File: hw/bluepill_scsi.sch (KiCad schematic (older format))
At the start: 14 parts, among them J1 Micro_SD_Card, J2 Conn_02x25_Odd_Even, J3 Programming Pins, J4 Berg Power Connector, U1 BluePill_STM32F103C

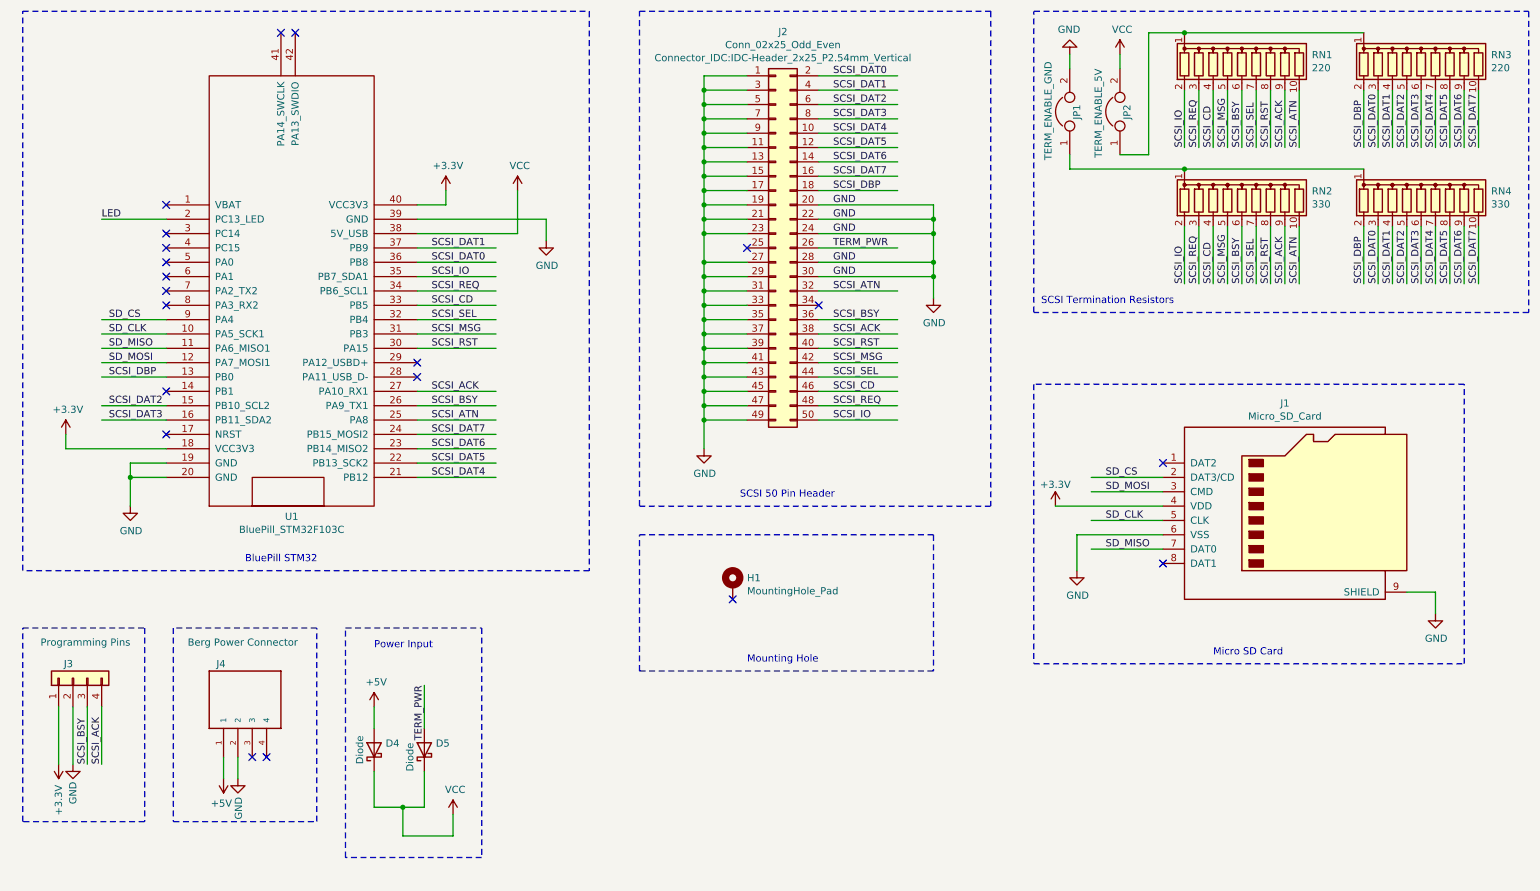
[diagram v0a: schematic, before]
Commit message: Added rough cut of STM32
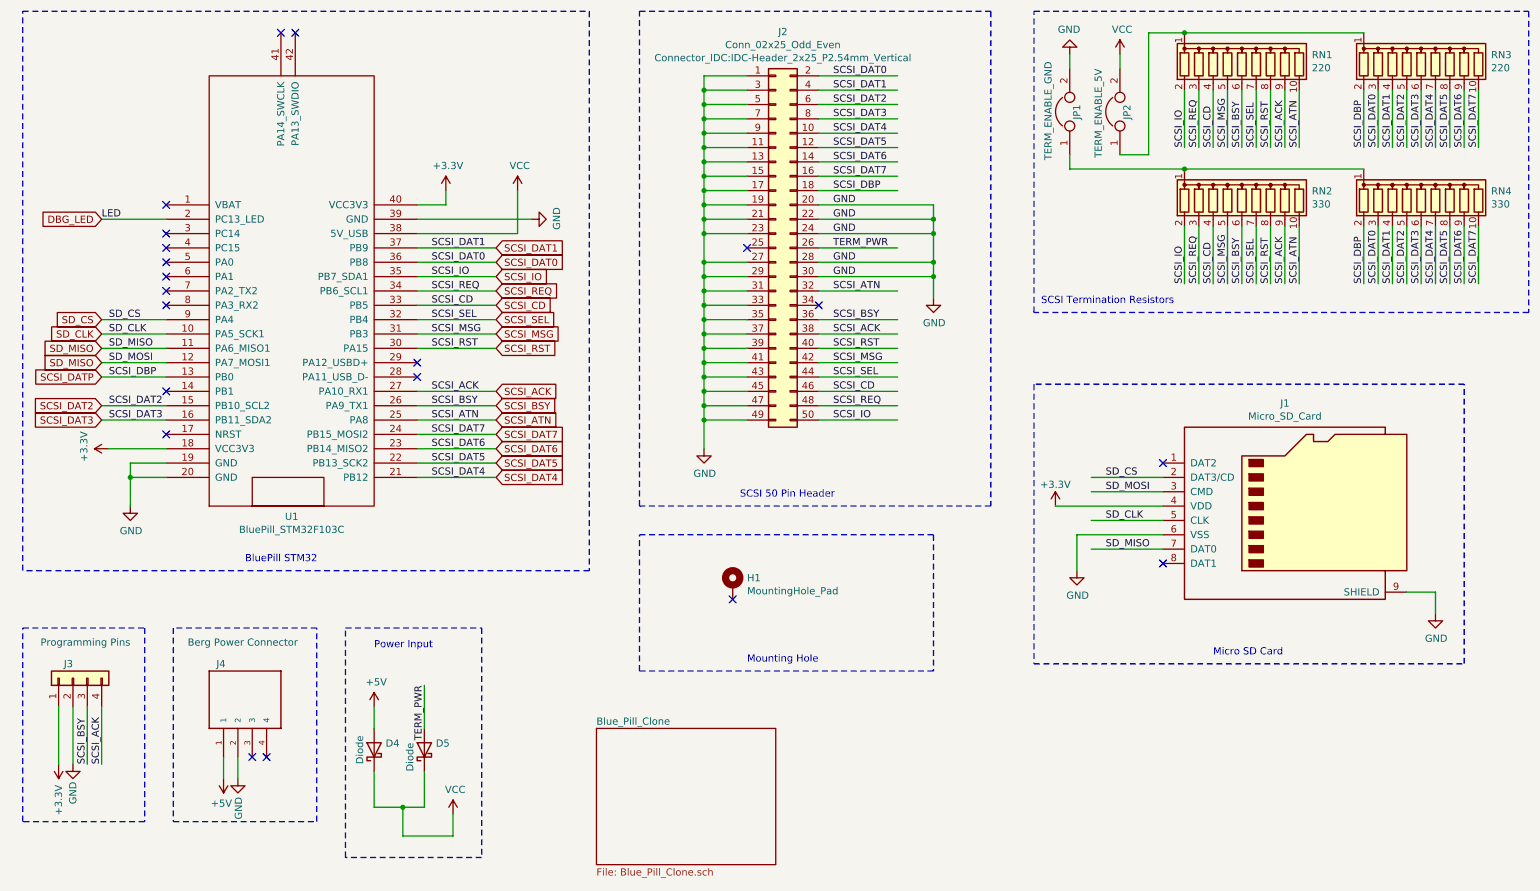
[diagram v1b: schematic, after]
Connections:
- net labels added: DBG_LED, SCSI_DATP
- wire segments 181 -> 179
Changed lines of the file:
@@
 $Descr A4 11693 8268
 encoding utf-8
-Sheet 1 1
+Sheet 1 2
 Title ""
 Date ""
@@
 	3550 2050 3550 1950
 Wire Wire Line
-	3350 2150 4250 2150
-Wire Wire Line
-	4250 2150 4250 2300
+	3350 2150 4150 2150
 $Comp
 L power:GND #PWR0104
 U 1 1 5F05BD87
-P 4250 2300
-F 0 "#PWR0104" H 4250 2050 50  0001 C CNN
-F 1 "GND" H 4255 2127 50  0000 C CNN
-F 2 "" H 4250 2300 50  0001 C CNN
-F 3 "" H 4250 2300 50  0001 C CNN
-	1    4250 2300
-	1    0    0    -1
+P 4150 2150
+F 0 "#PWR0104" H 4150 1900 50  0001 C CNN
+F 1 "GND" H 4155 1977 50  0000 C CNN
+F 2 "" H 4150 2150 50  0001 C CNN
+F 3 "" H 4150 2150 50  0001 C CNN
+	1    4150 2150
+	0    -1   -1   0
 $EndComp
 $Comp
@@
 	1    0    0    -1
 $EndComp
-Wire Wire Line
-	1600 3750 900  3750
-Wire Wire Line
-	900  3750 900  3650
 $Comp
 L power:+3.3V #PWR0107
 U 1 1 5F05ECF2
-P 900 3650
-F 0 "#PWR0107" H 900 3500 50  0001 C CNN
-F 1 "+3.3V" H 915 3823 50  0000 C CNN
-F 2 "" H 900 3650 50  0001 C CNN
-F 3 "" H 900 3650 50  0001 C CNN
-	1    900  3650
-	1    0    0    -1
+P 1200 3750
+F 0 "#PWR0107" H 1200 3600 50  0001 C CNN
+F 1 "+3.3V" H 1215 3923 50  0000 C CNN
+F 2 "" H 1200 3750 50  0001 C CNN
+F 3 "" H 1200 3750 50  0001 C CNN
+	1    1200 3750
+	0    -1   -1   0
 $EndComp
 Wire Wire Line
@@
 $EndComp
 $Comp
-L power:VCC #PWR?
+L power:VCC #PWR0112
 U 1 1 60659E21
 P 8250 1000
-F 0 "#PWR?" H 8250 850 50  0001 C CNN
+F 0 "#PWR0112" H 8250 850 50  0001 C CNN
 F 1 "VCC" H 8265 1173 50  0000 C CNN
 F 2 "" H 8250 1000 50  0001 C CNN
@@
 Wire Wire Line
 	8250 1000 8250 1100
+$Sheet
+S 4600 5700 1250 950
+U 60A49332
+F0 "Blue_Pill_Clone" 50
+F1 "Blue_Pill_Clone.sch" 50
+$EndSheet
+Text GLabel 3900 2350 2    50   Input ~ 0
+SCSI_DAT1
+Text GLabel 3900 2450 2    50   Input ~ 0
+SCSI_DAT0
+Text GLabel 3900 2550 2    50   Input ~ 0
+SCSI_IO
+Text GLabel 3900 2650 2    50   Input ~ 0
+SCSI_REQ
+Text GLabel 3900 2750 2    50   Input ~ 0
+SCSI_CD
+Text GLabel 3900 2850 2    50   Input ~ 0
+SCSI_SEL
+Text GLabel 3900 2950 2    50   Input ~ 0
+SCSI_MSG
+Text GLabel 3900 3050 2    50   Input ~ 0
+SCSI_RST
+Text GLabel 3900 3350 2    50   Input ~ 0
+SCSI_ACK
+Text GLabel 3900 3450 2    50   Input ~ 0
+SCSI_BSY
+Text GLabel 3900 3550 2    50   Input ~ 0
+SCSI_ATN
+Text GLabel 3900 3650 2    50   Input ~ 0
+SCSI_DAT7
+Text GLabel 3900 3750 2    50   Input ~ 0
+SCSI_DAT6
+Text GLabel 3900 3850 2    50   Input ~ 0
+SCSI_DAT5
+Text GLabel 3900 3950 2    50   Input ~ 0
+SCSI_DAT4
+Text GLabel 1150 2850 0    50   Input ~ 0
+SD_CS
+Text GLabel 1150 2950 0    50   Input ~ 0
+SD_CLK
+Text GLabel 1150 3050 0    50   Input ~ 0
+SD_MISO
+Text GLabel 1150 3150 0    50   Input ~ 0
+SD_MISO
+Text GLabel 1150 3250 0    50   Input ~ 0
+SCSI_DATP
+Text GLabel 1150 3450 0    50   Input ~ 0
+SCSI_DAT2
+Text GLabel 1150 3550 0    50   Input ~ 0
+SCSI_DAT3
+Wire Wire Line
+	1200 3750 1600 3750
+Text GLabel 1150 2150 0    50   Input ~ 0
+DBG_LED
 $EndSCHEMATC

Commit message: Updated bluepill all-in-one
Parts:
- renumbered D4 to D3, D5 to D4, J3 to J1, J2 to J5, J1 to J6, U1 to U3
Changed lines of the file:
@@
 $EndDescr
 $Comp
-L Connector_Generic:Conn_02x25_Odd_Even J2
+L Connector_Generic:Conn_02x25_Odd_Even J5
 U 1 1 5F0261A7
 P 5850 2350
-F 0 "J2" H 5900 3857 50  0000 C CNN
+F 0 "J5" H 5900 3857 50  0000 C CNN
 F 1 "Conn_02x25_Odd_Even" H 5900 3766 50  0000 C CNN
 F 2 "Connector_IDC:IDC-Header_2x25_P2.54mm_Vertical" H 5900 3675 50  0000 C CNN
@@
 	1350 3950 1350 4150
 $Comp
-L power:GND #PWR0102
+L power:GND #PWR04
 U 1 1 5F054918
 P 1350 4150
-F 0 "#PWR0102" H 1350 3900 50  0001 C CNN
+F 0 "#PWR04" H 1350 3900 50  0001 C CNN
 F 1 "GND" H 1355 3977 50  0000 C CNN
 F 2 "" H 1350 4150 50  0001 C CNN
@@
 	3350 2150 4150 2150
 $Comp
-L power:GND #PWR0104
+L power:GND #PWR011
 U 1 1 5F05BD87
 P 4150 2150
-F 0 "#PWR0104" H 4150 1900 50  0001 C CNN
+F 0 "#PWR011" H 4150 1900 50  0001 C CNN
 F 1 "GND" H 4155 1977 50  0000 C CNN
 F 2 "" H 4150 2150 50  0001 C CNN
@@
 $EndComp
 $Comp
-L power:+3.3V #PWR0106
+L power:+3.3V #PWR08
 U 1 1 5F05CE0E
 P 3550 1950
-F 0 "#PWR0106" H 3550 1800 50  0001 C CNN
+F 0 "#PWR08" H 3550 1800 50  0001 C CNN
 F 1 "+3.3V" H 3565 2123 50  0000 C CNN
 F 2 "" H 3550 1950 50  0001 C CNN
@@
 $EndComp
 $Comp
-L power:+3.3V #PWR0107
+L power:+3.3V #PWR03
 U 1 1 5F05ECF2
 P 1200 3750
-F 0 "#PWR0107" H 1200 3600 50  0001 C CNN
+F 0 "#PWR03" H 1200 3600 50  0001 C CNN
 F 1 "+3.3V" H 1215 3923 50  0000 C CNN
 F 2 "" H 1200 3750 50  0001 C CNN
@@
 SD_CS
 $Comp
-L power:+3.3V #PWR0108
+L power:+3.3V #PWR014
 U 1 1 5F08F209
 P 7800 4150
-F 0 "#PWR0108" H 7800 4000 50  0001 C CNN
+F 0 "#PWR014" H 7800 4000 50  0001 C CNN
 F 1 "+3.3V" H 7800 4300 50  0000 C CNN
 F 2 "" H 7800 4150 50  0001 C CNN
@@
 	7950 4350 7950 4600
 $Comp
-L power:GND #PWR0109
+L power:GND #PWR016
 U 1 1 5F092548
 P 7950 4600
-F 0 "#PWR0109" H 7950 4350 50  0001 C CNN
+F 0 "#PWR016" H 7950 4350 50  0001 C CNN
 F 1 "GND" H 7955 4427 50  0000 C CNN
 F 2 "" H 7950 4600 50  0001 C CNN
@@
 $EndComp
 $Comp
-L bluepill_scsi-rescue:BluePill_STM32F103C-bluepill U1
+L bluepill_scsi-rescue:BluePill_STM32F103C-bluepill U3
 U 1 1 5F01A526
 P 2450 2750
-F 0 "U1" H 2475 1277 50  0000 C CNN
+F 0 "U3" H 2475 1277 50  0000 C CNN
 F 1 "BluePill_STM32F103C" H 2475 1186 50  0000 C CNN
 F 2 "blue:BluePill_STM32F103C" H 2500 1150 50  0001 C CNN
@@
 $EndComp
 $Comp
-L Connector:Micro_SD_Card J1
+L Connector:Micro_SD_Card J6
 U 1 1 5F0BA382
 P 9450 4150
-F 0 "J1" H 9400 4867 50  0000 C CNN
+F 0 "J6" H 9400 4867 50  0000 C CNN
 F 1 "Micro_SD_Card" H 9400 4776 50  0000 C CNN
 F 2 "Connector_Card:microSD_HC_Molex_104031-0811" H 10600 4450 50  0001 C CNN
@@
 	10450 4750 10450 4900
 $Comp
-L power:GND #PWR0110
+L power:GND #PWR018
 U 1 1 5F0D8D42
 P 10450 4900
-F 0 "#PWR0110" H 10450 4650 50  0001 C CNN
+F 0 "#PWR018" H 10450 4650 50  0001 C CNN
 F 1 "GND" H 10455 4727 50  0000 C CNN
 F 2 "" H 10450 4900 50  0001 C CNN
@@
 Connection ~ 6950 2550
 $Comp
-L power:GND #PWR0116
+L power:GND #PWR013
 U 1 1 5F2D285F
 P 6950 2700
-F 0 "#PWR0116" H 6950 2450 50  0001 C CNN
+F 0 "#PWR013" H 6950 2450 50  0001 C CNN
 F 1 "GND" H 6955 2527 50  0000 C CNN
 F 2 "" H 6950 2700 50  0001 C CNN
@@
 $EndComp
 $Comp
-L power:GND #PWR0111
+L power:GND #PWR015
 U 1 1 5F9B6506
 P 7900 1000
-F 0 "#PWR0111" H 7900 750 50  0001 C CNN
+F 0 "#PWR015" H 7900 750 50  0001 C CNN
 F 1 "GND" H 7905 827 50  0000 C CNN
 F 2 "" H 7900 1000 50  0001 C CNN
@@
 	5350 3550 5350 3750
 $Comp
-L power:GND #PWR0101
+L power:GND #PWR012
 U 1 1 5F0440B9
 P 5350 3750
-F 0 "#PWR0101" H 5350 3500 50  0001 C CNN
+F 0 "#PWR012" H 5350 3500 50  0001 C CNN
 F 1 "GND" H 5355 3577 50  0000 C CNN
 F 2 "" H 5350 3750 50  0001 C CNN
@@
 	8700 850  9950 850
 $Comp
-L Connector_Generic:Conn_01x04 J3
+L Connector_Generic:Conn_01x04 J1
 U 1 1 5F8E1558
 P 950 5350
-F 0 "J3" V 1050 5350 50  0000 L CNN
+F 0 "J1" V 1050 5350 50  0000 L CNN
 F 1 "Programming Pins" V 1200 4950 50  0000 L CNN
 F 2 "Connector_PinHeader_2.54mm:PinHeader_1x04_P2.54mm_Vertical" H 950 5350 50  0001 C CNN
@@
 SCSI_BSY
 $Comp
-L power:GND #PWR0113
+L power:GND #PWR02
 U 1 1 5F92A76C
 P 950 5950
-F 0 "#PWR0113" H 950 5700 50  0001 C CNN
+F 0 "#PWR02" H 950 5700 50  0001 C CNN
 F 1 "GND" V 950 5750 50  0000 C CNN
 F 2 "" H 950 5950 50  0001 C CNN
@@
 $EndComp
 $Comp
-L power:+3.3V #PWR0114
+L power:+3.3V #PWR01
 U 1 1 5F92B1C2
 P 850 5950
-F 0 "#PWR0114" H 850 5800 50  0001 C CNN
+F 0 "#PWR01" H 850 5800 50  0001 C CNN
 F 1 "+3.3V" V 850 6200 50  0000 C CNN
 F 2 "" H 850 5950 50  0001 C CNN
@@
 	600  6350 600  5000
 $Comp
-L power:GND #PWR0117
+L power:GND #PWR06
 U 1 1 5F9CFB24
 P 2100 6050
-F 0 "#PWR0117" H 2100 5800 50  0001 C CNN
+F 0 "#PWR06" H 2100 5800 50  0001 C CNN
 F 1 "GND" V 2105 5922 50  0000 R CNN
 F 2 "" H 2100 6050 50  0001 C CNN
@@
 TERM_PWR
 $Comp
-L power:+5V #PWR0103
+L power:+5V #PWR07
 U 1 1 5FB28DFC
 P 3050 5550
-F 0 "#PWR0103" H 3050 5400 50  0001 C CNN
+F 0 "#PWR07" H 3050 5400 50  0001 C CNN
 F 1 "+5V" H 3065 5723 50  0000 C CNN
 F 2 "" H 3050 5550 50  0001 C CNN
@@
 $EndComp
 $Comp
-L power:VCC #PWR0105
+L power:VCC #PWR09
 U 1 1 5FB29B44
 P 3600 6300
-F 0 "#PWR0105" H 3600 6150 50  0001 C CNN
+F 0 "#PWR09" H 3600 6150 50  0001 C CNN
 F 1 "VCC" H 3615 6473 50  0000 C CNN
 F 2 "" H 3600 6300 50  0001 C CNN
@@
 	6150 2350 6700 2350
 $Comp
-L power:VCC #PWR0115
+L power:VCC #PWR010
 U 1 1 5FB9CE9F
 P 4050 1950
-F 0 "#PWR0115" H 4050 1800 50  0001 C CNN
+F 0 "#PWR010" H 4050 1800 50  0001 C CNN
 F 1 "VCC" H 4065 2123 50  0000 C CNN
 F 2 "" H 4050 1950 50  0001 C CNN
@@
 $EndComp
 $Comp
-L power:+5V #PWR0119
+L power:+5V #PWR05
 U 1 1 5FBE27DC
 P 2000 6050
-F 0 "#PWR0119" H 2000 5900 50  0001 C CNN
+F 0 "#PWR05" H 2000 5900 50  0001 C CNN
 F 1 "+5V" H 2015 6223 50  0000 C CNN
 F 2 "" H 2000 6050 50  0001 C CNN
@@
 $EndComp
 $Comp
-L Device:D_Schottky D4
+L Device:D_Schottky D3
 U 1 1 5FB96EB2
 P 3050 5850
-F 0 "D4" V 3096 5770 50  0000 R CNN
+F 0 "D3" V 3096 5770 50  0000 R CNN
 F 1 "Diode" H 3150 5950 50  0000 R CNN
 F 2 "Diode_THT:D_A-405_P7.62mm_Horizontal" H 3050 5850 50  0001 C CNN
@@
 $EndComp
 $Comp
-L Device:D_Schottky D5
+L Device:D_Schottky D4
 U 1 1 5FB97E4B
 P 3400 5850
-F 0 "D5" V 3446 5770 50  0000 R CNN
+F 0 "D4" V 3446 5770 50  0000 R CNN
 F 1 "Diode" H 3450 5950 50  0000 R CNN
 F 2 "Diode_THT:D_A-405_P7.62mm_Horizontal" H 3400 5850 50  0001 C CNN
@@
 $EndComp
 $Comp
-L power:VCC #PWR0112
+L power:VCC #PWR017
 U 1 1 60659E21
 P 8250 1000
-F 0 "#PWR0112" H 8250 850 50  0001 C CNN
+F 0 "#PWR017" H 8250 850 50  0001 C CNN
 F 1 "VCC" H 8265 1173 50  0000 C CNN
 F 2 "" H 8250 1000 50  0001 C CNN
@@
 S 4600 5700 1250 950
 U 60A49332
-F0 "Blue_Pill_Clone" 50
+F0 "Onboard Blue Pil" 50
 F1 "Blue_Pill_Clone.sch" 50
 $EndSheet

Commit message: As-ordered version
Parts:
- removed D3, D4: Diode, Diode_THT:D_A-405_P7.62mm_Horizontal, symbol Device:D_Schottky
- removed J1: Programming Pins, Connector_PinHeader_2.54mm:PinHeader_1x04_P2.54mm_Vertical, symbol Connector_Generic:Conn_01x04
- removed RN1, RN3: 220, Resistor_THT:R_Array_SIP10, symbol Device:R_Network09
- removed RN2, RN4: 330, Resistor_THT:R_Array_SIP10, symbol Device:R_Network09
- added C15, C17, C19, C21, C23, C25, C27, C29, C31, C33, C35, C37, C39, C41, C43, C45, C47, C49: 330, Resistor_SMD:R_0603_1608Metric, symbol Device:C_Small
- added C16, C18, C20, C22, C24, C26, C28, C30, C32, C34, C36, C38, C40, C42, C44, C46, C48, C8: 220, Resistor_SMD:R_0603_1608Metric, symbol Device:C_Small
- added D3, D4: SM4007PL, Diode_SMD:D_SOD-123F, symbol Device:D_Small
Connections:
- net labels added: BERG_5V
- wire segments 179 -> 207
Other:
- moved on the sheet: JP2

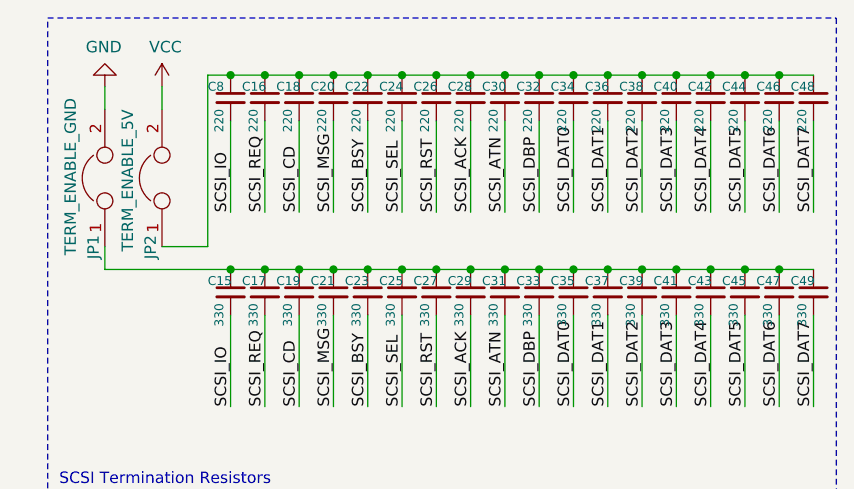
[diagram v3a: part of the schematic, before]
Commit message: Fixed resistor sizes. As-ordered Beta 3
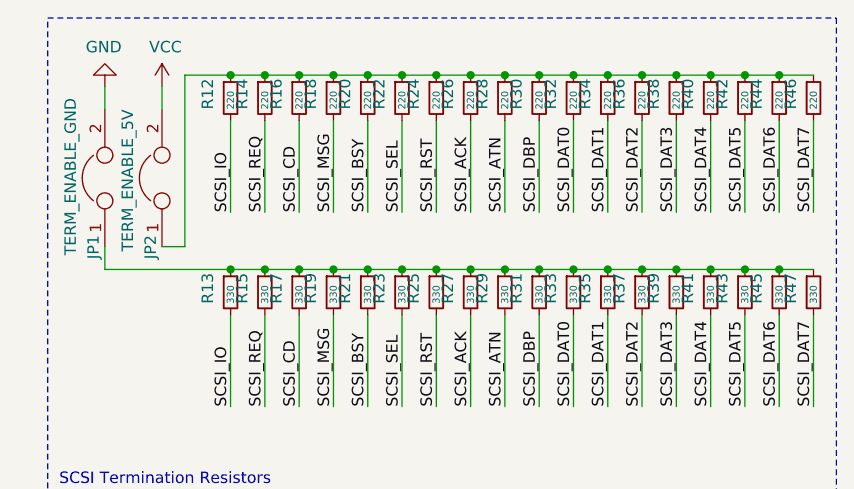
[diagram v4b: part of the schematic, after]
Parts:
- removed C15, C17, C19, C21, C23, C25, C27, C29, C31, C33, C35, C37, C39, C41, C43, C45, C47, C49: 330, Resistor_SMD:R_0603_1608Metric, symbol Device:C_Small
- removed C16, C18, C20, C22, C24, C26, C28, C30, C32, C34, C36, C38, C40, C42, C44, C46, C48, C8: 220, Resistor_SMD:R_0603_1608Metric, symbol Device:C_Small
- added R12, R14, R16, R18, R20, R22, R24, R26, R28, R30, R32, R34, R36, R38, R40, R42, R44, R46: 220, Resistor_SMD:R_0603_1608Metric, symbol Device:R_Small
- added R13, R15, R17, R19, R21, R23, R25, R27, R29, R31, R33, R35, R37, R39, R41, R43, R45, R47: 330, Resistor_SMD:R_0603_1608Metric, symbol Device:R_Small

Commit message: Fixes from integration. As-ordered 1.0
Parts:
- removed D3, D4: SM4007PL, Diode_SMD:D_SOD-123F, symbol Device:D_Small
- removed JP1: TERM_ENABLE_GND, Connector_PinSocket_2.54mm:PinSocket_1x02_P2.54mm_Vertical, symbol Device:Jumper
- removed JP2: TERM_ENABLE_5V, Connector_PinSocket_2.54mm:PinSocket_1x02_P2.54mm_Vertical, symbol Device:Jumper
- added D3, D4: D_Schottky, Diode_SMD:D_SOD-123, symbol Device:D_Schottky
- added J1: Conn_02x02_Odd_Even, Connector_PinHeader_2.54mm:PinHeader_2x02_P2.54mm_Vertical, symbol Connector_Generic:Conn_02x02_Odd_Even
- added TP10, TP11, TP12, TP13, TP6, TP7, TP8, TP9: TestPoint_Small, TestPoint:TestPoint_THTPad_D1.0mm_Drill0.5mm, symbol Connector:TestPoint_Small
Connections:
- net labels removed: +5V
- wire segments 207 -> 209
- no-connect marks 20 -> 18
